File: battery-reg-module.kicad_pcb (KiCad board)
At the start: 2 copper layers, 15.2 x 12.7 mm, 10 parts, among them J1 Conn_01x02_Pin, J2 Conn_01x02_Pin, U1 MIC2779H-1YM5-TR, U2 AP7362-33SP-13

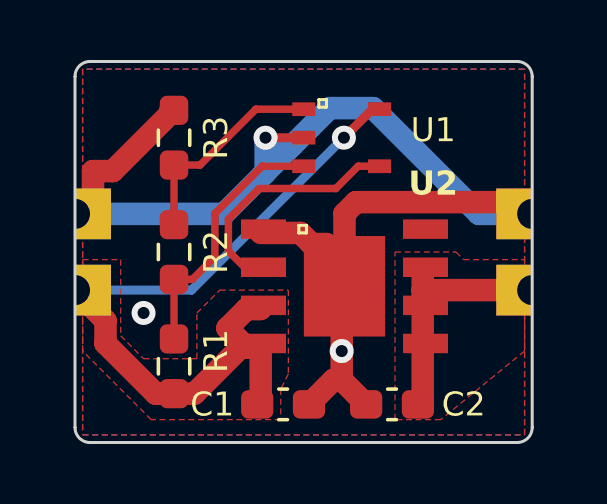
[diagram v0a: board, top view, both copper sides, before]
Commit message: Modify voltage monitor pad sizes, silkscreen, edit readme
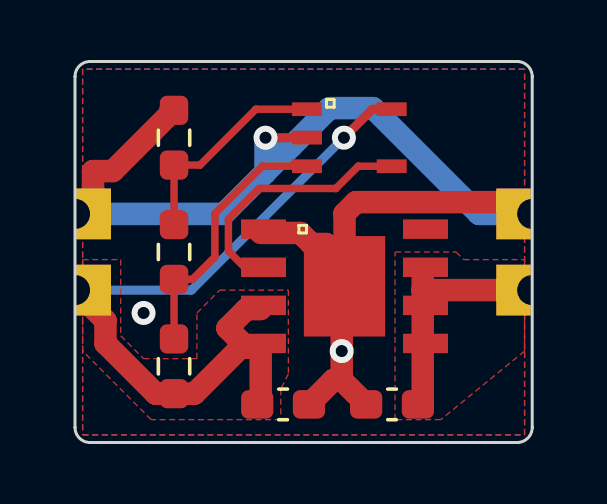
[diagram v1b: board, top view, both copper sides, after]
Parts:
- moved REF** 5.68 mm to (159.0, 128.3)
- moved U1 0.25 mm to (161.5, 121.9)
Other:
- board text added: "© JMG 2024"
